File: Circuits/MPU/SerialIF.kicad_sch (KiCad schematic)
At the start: 15 parts, among them U2 ADM3488ARZ, X1 KC2016K50.0000C1GE00

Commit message: Passes DRC
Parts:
- removed unit 8 of 	U1
- added unit 9 of U1
- C2: Spec 10WVDC X7R -> 50WVDC C0G
- U1: renamed from 	U1
- renumbered R6 to R1, R1 to R10, R7 to R2, R8 to R3, R9 to R4, R3 to R5, R4 to R6, R5 to R7, R10 to R8, R2 to R9
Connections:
- net at U2.3 (DI): now also U1.R5 (TX422)
- net at U2.2 (RO): now also U1.R6 (RX422)

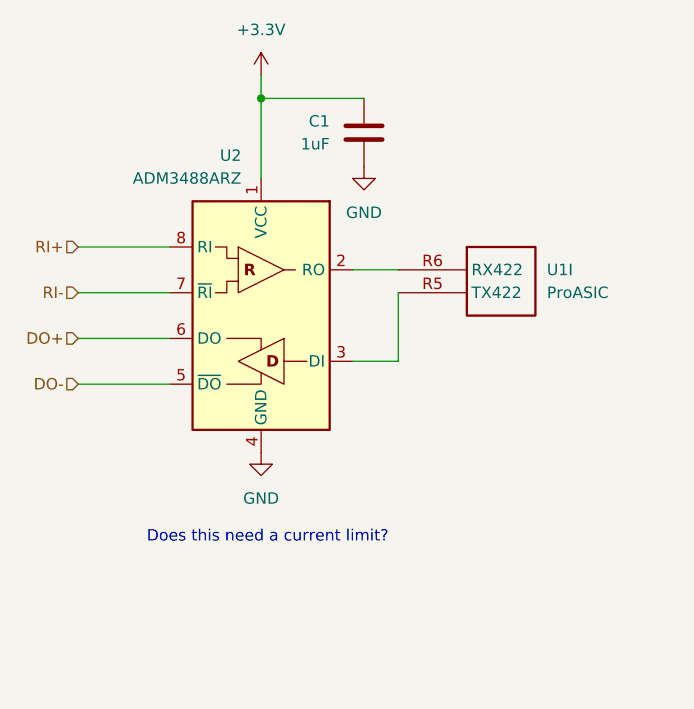
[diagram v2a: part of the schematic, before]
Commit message: CL resistor for RS422
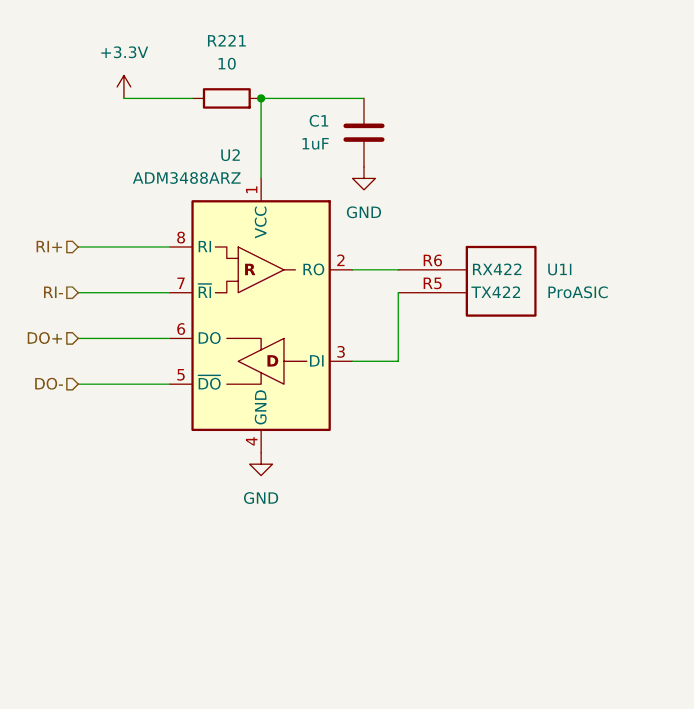
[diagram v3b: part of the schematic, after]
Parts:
- added R221: 10, Resistor_SMD:R_2512_6332Metric, symbol Device:R
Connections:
- net +3.3V: now also R221.1; no longer C1.1, U2.1 (VCC)
- new net: C1.1, R221.2, U2.1 (VCC)
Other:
- note removed: "Does this need a current limit?"

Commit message: bunch of little fixes
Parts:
- C2: Spec 50WVDC C0G -> 50WVDC X7R
- U1: footprint Package_BGA:BGA-484_23.0x23.0mm_Layout22x22_P1.0mm -> Package_BGA:BGA-484_23.0x23.0mm_Layout22x22_P1.0mm
- X1: footprint (none) -> Crystal:Crystal_SMD_2016-4Pin_2.0x1.6mm
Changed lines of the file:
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@@
 	(title_block
 		(title "QuERI MPU")
-		(date "2024-03-28")
+		(date "2024-05-26")
 		(rev "Draft")
 		(company "Noqsi Aerospace Ltd")
@@
 			)
 		)
-		(property "Spec" "50WVDC C0G"
+		(property "Spec" "50WVDC X7R"
 			(at 171.45 139.7 0)
 			(effects
@@
 			)
 		)
-		(property "Footprint" ""
+		(property "Footprint" "Crystal:Crystal_SMD_2016-4Pin_2.0x1.6mm"
 			(at 201.93 148.59 0)
 			(effects
@@
 			)
 		)
-		(property "Footprint" "	Package_BGA:BGA-484_23.0x23.0mm_Layout22x22_P1.0mm"
+		(property "Footprint" "Package_BGA:BGA-484_23.0x23.0mm_Layout22x22_P1.0mm"
 			(at 209.55 87.63 0)
 			(effects
@@
 			)
 		)
-		(property "Footprint" "	Package_BGA:BGA-484_23.0x23.0mm_Layout22x22_P1.0mm"
+		(property "Footprint" "Package_BGA:BGA-484_23.0x23.0mm_Layout22x22_P1.0mm"
 			(at 80.01 63.5 0)
 			(effects
